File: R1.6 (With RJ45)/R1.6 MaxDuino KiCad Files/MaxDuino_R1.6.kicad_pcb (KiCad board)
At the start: 2 copper layers, 99.8 x 49.8 mm, 66 parts, among them J1 15V AC/DC or DCC, J10 RS-485, J2 DCC Signal, J3 Vin_EN, J4 SPKR, J4-1 I/O, J4-2 +5, J4-3 GND, J5 SPKR, J5-1 I/O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

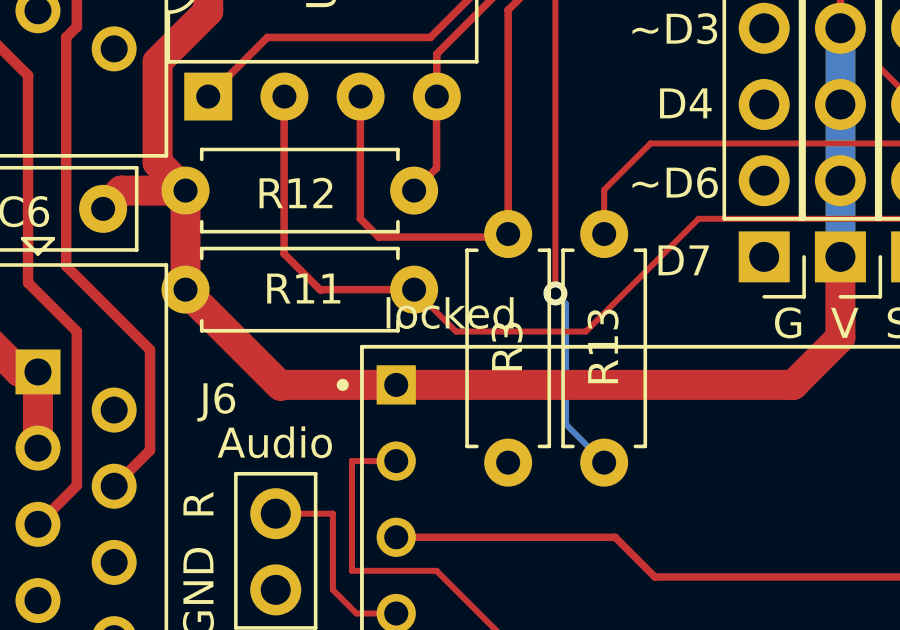
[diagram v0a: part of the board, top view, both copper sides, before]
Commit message: Documentation Improvements
Improved documentation, added photos.
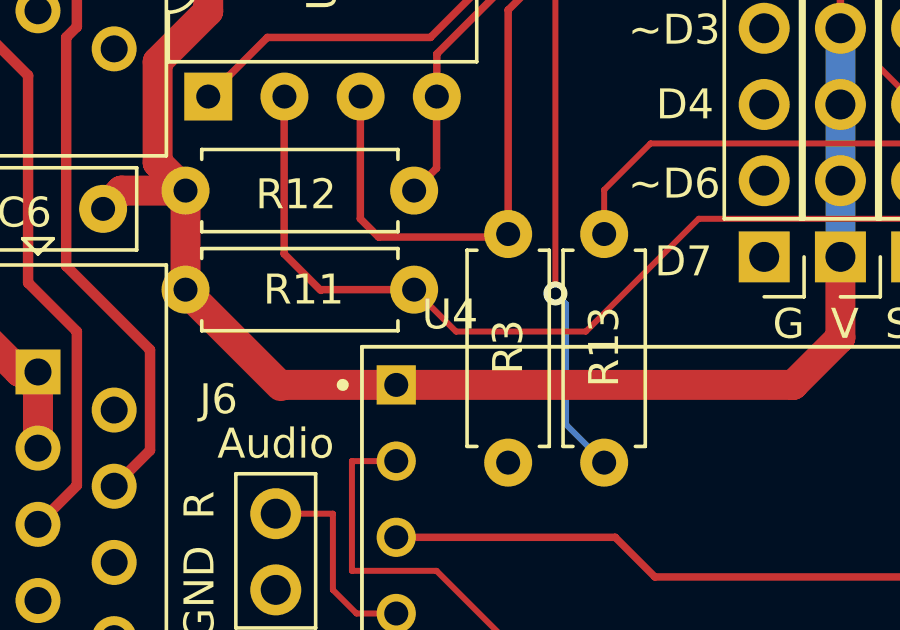
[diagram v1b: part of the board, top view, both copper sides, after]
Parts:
- renumbered locked to U4
